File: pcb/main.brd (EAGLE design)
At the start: 58 x 58 mm, 23 parts, among them Q1 MOSFET-NCHANNEL2N7000

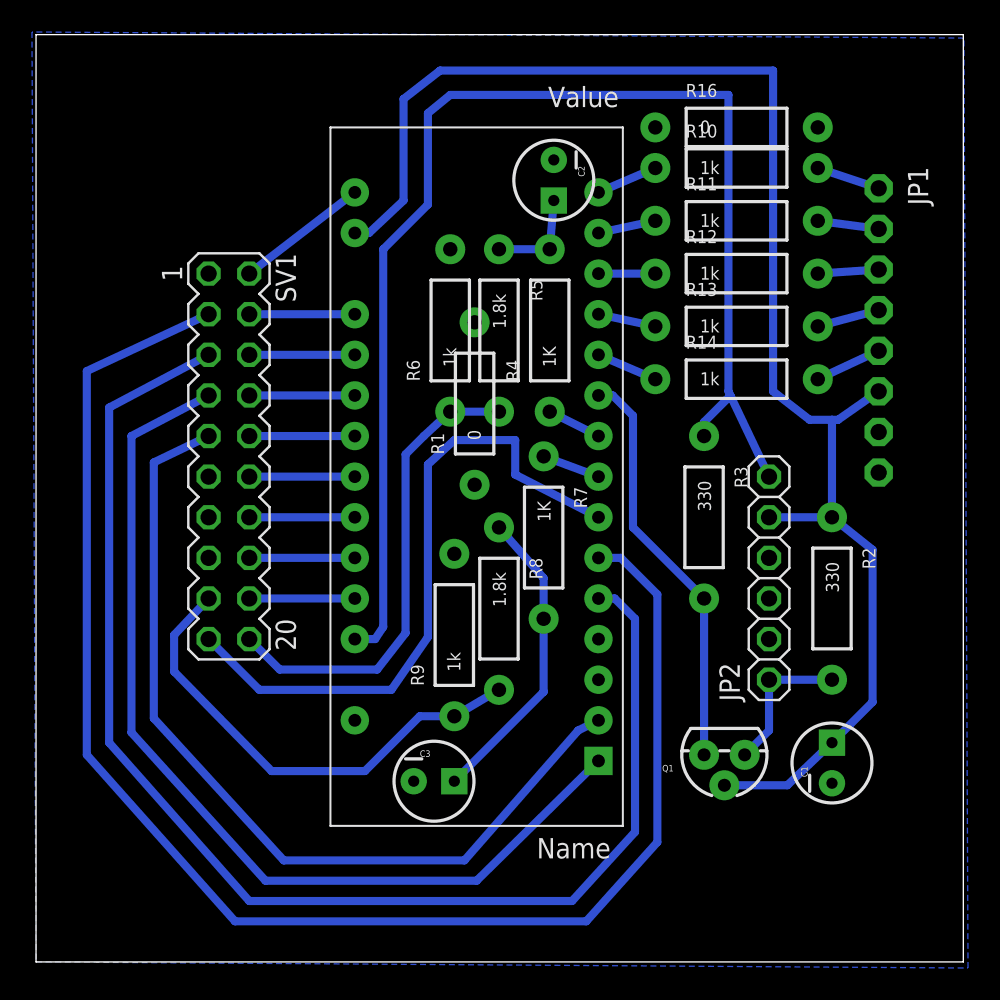
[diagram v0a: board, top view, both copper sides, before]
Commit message: updated low pass filter
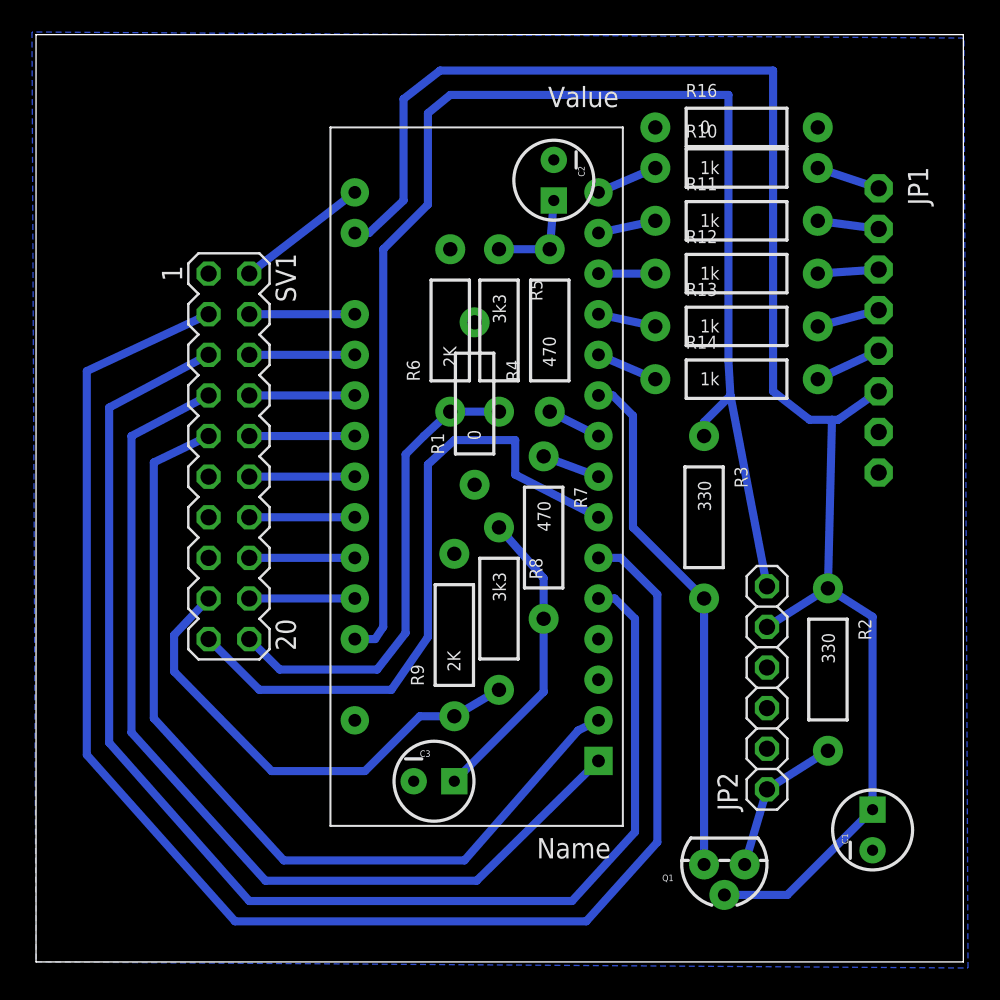
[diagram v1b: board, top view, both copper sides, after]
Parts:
- R4, R7: value 1K -> 470
- R5, R8: value 1.8k -> 3k3
- R6, R9: value 1k -> 2K
- moved JP2 6.86 mm to (45.7, 17.1)
- moved Q1 6.86 mm to (43.1, 6.10)
- moved C1 4.90 mm to (52.3, 8.26)
- moved R2 4.45 mm to (49.5, 18.3)
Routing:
- net 3.3V: track 96.0 -> 103.7 mm
- net DATA_5V: track 25.7 -> 32.6 mm
- net 5V: track 82.3 -> 88.8 mm
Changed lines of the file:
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@@
 <?xml version="1.0" encoding="utf-8"?>
 <!DOCTYPE eagle SYSTEM "eagle.dtd">
-<eagle version="6.5.0">
+<eagle version="7.1.0">
 <drawing>
 <settings>
@@
 <layer number="17" name="Pads" color="2" fill="1" visible="yes" active="yes"/>
 <layer number="18" name="Vias" color="2" fill="1" visible="yes" active="yes"/>
-<layer number="19" name="Unrouted" color="6" fill="1" visible="no" active="yes"/>
-<layer number="20" name="Dimension" color="15" fill="1" visible="no" active="yes"/>
-<layer number="21" name="tPlace" color="7" fill="1" visible="no" active="yes"/>
-<layer number="22" name="bPlace" color="7" fill="1" visible="no" active="yes"/>
-<layer number="23" name="tOrigins" color="15" fill="1" visible="no" active="yes"/>
-<layer number="24" name="bOrigins" color="15" fill="1" visible="no" active="yes"/>
-<layer number="25" name="tNames" color="7" fill="1" visible="no" active="yes"/>
-<layer number="26" name="bNames" color="7" fill="1" visible="no" active="yes"/>
-<layer number="27" name="tValues" color="7" fill="1" visible="no" active="yes"/>
-<layer number="28" name="bValues" color="7" fill="1" visible="no" active="yes"/>
+<layer number="19" name="Unrouted" color="6" fill="1" visible="yes" active="yes"/>
+<layer number="20" name="Dimension" color="15" fill="1" visible="yes" active="yes"/>
+<layer number="21" name="tPlace" color="7" fill="1" visible="yes" active="yes"/>
+<layer number="22" name="bPlace" color="7" fill="1" visible="yes" active="yes"/>
+<layer number="23" name="tOrigins" color="15" fill="1" visible="yes" active="yes"/>
+<layer number="24" name="bOrigins" color="15" fill="1" visible="yes" active="yes"/>
+<layer number="25" name="tNames" color="7" fill="1" visible="yes" active="yes"/>
+<layer number="26" name="bNames" color="7" fill="1" visible="yes" active="yes"/>
+<layer number="27" name="tValues" color="7" fill="1" visible="yes" active="yes"/>
+<layer number="28" name="bValues" color="7" fill="1" visible="yes" active="yes"/>
 <layer number="29" name="tStop" color="7" fill="3" visible="no" active="yes"/>
 <layer number="30" name="bStop" color="7" fill="6" visible="no" active="yes"/>
@@
 <pass name="Default">
 <param name="RoutingGrid" value="50mil"/>
+<param name="AutoGrid" value="1"/>
+<param name="Efforts" value="0"/>
+<param name="TopRouterVariant" value="1"/>
 <param name="tpViaShape" value="round"/>
 <param name="PrefDir.1" value="|"/>
@@
 </autorouter>
 <elements>
-<element name="Q1" library="SparkFun-DiscreteSemi" package="TO-92" value="MOSFET-NCHANNEL2N7000" x="43.053" y="12.954" rot="R180"/>
+<element name="Q1" library="SparkFun-DiscreteSemi" package="TO-92" value="MOSFET-NCHANNEL2N7000" x="43.053" y="6.096" rot="R180"/>
 <element name="SV1" library="con-lstb" package="MA10-2" value="to_3ds" x="12.065" y="31.623" rot="R270">
 <attribute name="OC_NEWARK" value="unknown" x="-42.545" y="4.953" size="1.778" layer="27" rot="R270" display="off"/>
@@
 <attribute name="OC_FARNELL" value="unknown" x="-42.545" y="4.953" size="1.778" layer="27" rot="R270" display="off"/>
 </element>
-<element name="C1" library="SparkFun-Capacitors" package="CPOL-RADIAL-10UF-25V" value="1uf" x="49.784" y="12.446" rot="R90"/>
+<element name="C1" library="SparkFun-Capacitors" package="CPOL-RADIAL-10UF-25V" value="1uf" x="52.324" y="8.255" rot="R90"/>
 <element name="JP1" library="adafruit" package="1X08-CLEANBIG" value="nokia_lcd" x="52.705" y="39.497" rot="R270"/>
-<element name="R2" library="SparkFun-Resistors" package="AXIAL-0.4" value="330" x="49.784" y="22.733" rot="R270"/>
+<element name="R2" library="SparkFun-Resistors" package="AXIAL-0.4" value="330" x="49.53" y="18.288" rot="R270"/>
 <element name="R3" library="SparkFun-Resistors" package="AXIAL-0.4" value="330" x="41.783" y="27.813" rot="R270"/>
-<element name="R4" library="SparkFun-Resistors" package="AXIAL-0.4" value="1K" x="32.131" y="39.497" rot="R90"/>
+<element name="R4" library="SparkFun-Resistors" package="AXIAL-0.4" value="470" x="32.131" y="39.497" rot="R90"/>
 <element name="C2" library="SparkFun-Capacitors" package="CPOL-RADIAL-10UF-25V" value="1uF" x="32.385" y="48.895" rot="R270"/>
-<element name="R5" library="SparkFun-Resistors" package="AXIAL-0.4" value="1.8k" x="28.956" y="39.497" rot="R270"/>
-<element name="R6" library="SparkFun-Resistors" package="AXIAL-0.4" value="1k" x="25.908" y="39.497" rot="R90"/>
-<element name="R7" library="SparkFun-Resistors" package="AXIAL-0.4" value="1K" x="31.75" y="26.543" rot="R270"/>
+<element name="R5" library="SparkFun-Resistors" package="AXIAL-0.4" value="3k3" x="28.956" y="39.497" rot="R270"/>
+<element name="R6" library="SparkFun-Resistors" package="AXIAL-0.4" value="2K" x="25.908" y="39.497" rot="R90"/>
+<element name="R7" library="SparkFun-Resistors" package="AXIAL-0.4" value="470" x="31.75" y="26.543" rot="R270"/>
 <element name="C3" library="SparkFun-Capacitors" package="CPOL-RADIAL-10UF-25V" value="1uF" x="24.892" y="11.303"/>
-<element name="R8" library="SparkFun-Resistors" package="AXIAL-0.4" value="1.8k" x="28.956" y="22.098" rot="R270"/>
-<element name="R9" library="SparkFun-Resistors" package="AXIAL-0.4" value="1k" x="26.162" y="20.447" rot="R90"/>
+<element name="R8" library="SparkFun-Resistors" package="AXIAL-0.4" value="3k3" x="28.956" y="22.098" rot="R270"/>
+<element name="R9" library="SparkFun-Resistors" package="AXIAL-0.4" value="2K" x="26.162" y="20.447" rot="R90"/>
 <element name="R10" library="SparkFun-Resistors" package="AXIAL-0.4" value="1k" x="43.815" y="49.657"/>
 <element name="R11" library="SparkFun-Resistors" package="AXIAL-0.4" value="1k" x="43.815" y="46.355"/>
@@
 <element name="R14" library="SparkFun-Resistors" package="AXIAL-0.4" value="1k" x="43.815" y="36.449"/>
 <element name="U$1" library="nano" package="PDIP-32" value="ARDUINONANO" x="35.179" y="10.033" rot="R180"/>
-<element name="JP2" library="adafruit" package="1X06" value="gc_controller" x="45.847" y="24.003" rot="R90"/>
+<element name="JP2" library="adafruit" package="1X06" value="gc_controller" x="45.72" y="17.145" rot="R90"/>
 <element name="R16" library="SparkFun-Resistors" package="AXIAL-0.4" value="0" x="43.815" y="52.197"/>
 <element name="R1" library="SparkFun-Resistors" package="AXIAL-0.4" value="0" x="27.432" y="34.925" rot="R90"/>
@@
 <contactref element="R1" pad="P$2"/>
 <wire x1="27.432" y1="40.005" x2="27.432" y2="29.845" width="0" layer="19" extent="1-1"/>
-<wire x1="52.705" y1="30.607" x2="45.847" y2="25.273" width="0" layer="19" extent="1-1"/>
+<wire x1="52.324" y1="6.985" x2="45.72" y2="13.335" width="0" layer="19" extent="1-1"/>
 </signal>
 <signal name="5V">
@@
 <wire x1="24.511" y1="53.086" x2="25.908" y2="54.229" width="0.508" layer="16"/>
 <wire x1="25.908" y1="54.229" x2="43.307" y2="54.229" width="0.508" layer="16"/>
-<wire x1="43.307" y1="54.229" x2="43.307" y2="35.687" width="0.508" layer="16"/>
+<wire x1="43.307" y1="54.229" x2="43.307" y2="37.592" width="0.508" layer="16"/>
 <contactref element="JP2" pad="6"/>
-<wire x1="43.307" y1="35.687" x2="43.433765625" y2="35.42079375" width="0.508" layer="16"/>
-<wire x1="43.433765625" y1="35.42079375" x2="45.847" y2="30.353" width="0.508" layer="16"/>
+<wire x1="43.307" y1="37.592" x2="43.433765625" y2="35.42079375" width="0.508" layer="16"/>
+<wire x1="43.433765625" y1="35.42079375" x2="45.72" y2="23.495" width="0.508" layer="16"/>
 <wire x1="41.783" y1="32.893" x2="41.783" y2="33.770028125" width="0.508" layer="16"/>
 <wire x1="41.783" y1="33.770028125" x2="43.433765625" y2="35.42079375" width="0.508" layer="16"/>
@@
 <wire x1="50.165" y1="33.909" x2="52.705" y2="35.687" width="0.508" layer="16"/>
 <contactref element="JP2" pad="5"/>
-<wire x1="49.784" y1="27.813" x2="49.784" y2="33.909" width="0.508" layer="16"/>
-<wire x1="45.847" y1="27.813" x2="49.784" y2="27.813" width="0.508" layer="16"/>
-<wire x1="43.053" y1="11.049" x2="46.99" y2="11.049" width="0.508" layer="16"/>
-<wire x1="52.324" y1="25.781" x2="49.784" y2="27.813" width="0.508" layer="16"/>
+<wire x1="49.53" y1="23.368" x2="49.784" y2="33.909" width="0.508" layer="16"/>
+<wire x1="45.72" y1="20.955" x2="49.53" y2="23.368" width="0.508" layer="16"/>
 <contactref element="C1" pad="1"/>
-<wire x1="49.784" y1="13.716" x2="46.99" y2="11.049" width="0.508" layer="16"/>
-<wire x1="52.324" y1="25.781" x2="52.324" y2="16.256" width="0.508" layer="16"/>
-<wire x1="52.324" y1="16.256" x2="49.784" y2="13.716" width="0.508" layer="16"/>
+<wire x1="43.053" y1="4.191" x2="46.99" y2="4.191" width="0.508" layer="16"/>
+<wire x1="46.99" y1="4.191" x2="52.324" y2="9.525" width="0.508" layer="16"/>
+<wire x1="52.324" y1="9.525" x2="52.324" y2="21.59" width="0.508" layer="16"/>
+<wire x1="52.324" y1="21.59" x2="49.53" y2="23.368" width="0.508" layer="16"/>
 </signal>
 <signal name="DATA_3V3">
@@
 <contactref element="Q1" pad="1"/>
 <contactref element="JP2" pad="1"/>
-<wire x1="45.847" y1="17.653" x2="49.784" y2="17.653" width="0.508" layer="16"/>
-<wire x1="45.847" y1="17.653" x2="45.847" y2="14.478" width="0.508" layer="16"/>
-<wire x1="45.847" y1="14.478" x2="44.323" y2="12.954" width="0.508" layer="16"/>
+<wire x1="49.53" y1="13.208" x2="45.72" y2="10.795" width="0.508" layer="16"/>
+<wire x1="45.72" y1="10.795" x2="44.323" y2="6.096" width="0.508" layer="16"/>
 </signal>
 <signal name="DATA_5V">
@@
 <contactref element="R3" pad="P$2"/>
 <contactref element="U$1" pad="D7"/>
-<wire x1="41.783" y1="22.733" x2="41.783" y2="12.954" width="0.508" layer="16"/>
+<wire x1="41.783" y1="22.733" x2="41.783" y2="6.096" width="0.508" layer="16"/>
 <wire x1="35.179" y1="35.433" x2="36.068" y2="35.433" width="0.508" layer="16"/>
 <wire x1="36.068" y1="35.433" x2="37.338" y2="34.163" width="0.508" layer="16"/>
